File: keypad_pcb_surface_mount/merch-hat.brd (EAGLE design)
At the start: 65 x 56 mm, 29 parts, among them U2 ATMEGA328P_TQFP, Y2 16MHZ

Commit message: Fixes and updates
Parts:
- removed GPIO1: PIN20X2, FLYFISH:PIN_20X2
- removed PORT: Sensor Port, pinhead:1X03
- added C3: 0.1uF, merch-hardware:0603-CAP
- added PORT_OUT: Sensor Port, pinhead:1X03
- added R14: 1k, merch-hardware:0603-RES
- added R15, R16: 3.9k, merch-hardware:0603-RES
- added U1: CAT24C32, merch-hardware:SO08
- added WP: (no value), pinhead:1X02
- D2: value 74LS155D -> 74LS156D
- R1, R10, R11, R12, R13, R2, R3, R4, R5, R6, R7, R8, R9: device resistor:R0805 -> merch-hardware:0603-RES
- moved C1 20.5 mm to (29.7, 10.9), turned to 270 degrees
- moved R12 6.31 mm to (26.2, 42.3), turned to 90 degrees
- moved R13 5.99 mm to (28.8, 42.3), turned to 90 degrees
- moved LIMITSWITCH 5.99 mm to (26.2, 46.4), turned to 0 degrees
- moved R11 4.94 mm to (23.1, 34.8)
- moved C2 2.22 mm to (30.9, 14.9)
- moved R1 0.38 mm to (61.5, 13.2)
- moved R2 0.38 mm to (61.5, 15.7)
- moved R3 0.38 mm to (61.5, 18.3)
- moved R4 0.38 mm to (61.5, 20.8)
- moved R5 0.38 mm to (61.5, 23.4)
- moved R6 0.38 mm to (61.5, 25.9)
- moved R7 0.38 mm to (61.5, 31.0)
- moved R8 0.38 mm to (61.5, 33.5)
- moved R9 0.38 mm to (61.5, 36.1)
- renumbered COL_DEMUX to D2, ROW_MUX to D1, SELECT_BITS to D3
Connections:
- new net N$2: R14.1, U1.7, WP.1
- net +5V: no longer GPIO1.2, GPIO1.4
- net 3.3V: now also C3.2, R14.2, R15.2, R16.2, U1.8; no longer GPIO1.1, GPIO1.17
- net GND: now also C3.1, D2.14, PORT_OUT.3, U1.1, U1.2, U1.3, U1.4, WP.2; no longer GPIO1.14, GPIO1.20, GPIO1.25, GPIO1.30, GPIO1.34, GPIO1.39, GPIO1.6, GPIO1.9, PORT.3
- net GPIO10: no longer GPIO1.19
- net GPIO11: no longer GPIO1.23
- net GPIO12: no longer GPIO1.32
- net GPIO13: no longer GPIO1.33
- net GPIO16: now also D3.11; no longer GPIO1.36
- net GPIO19: no longer GPIO1.35
- net GPIO2: no longer GPIO1.3
- net GPIO20: now also PORT_OUT.1; no longer GPIO1.38, PORT.1
- net GPIO21: no longer GPIO1.40
- net GPIO23: now also LIMITSWITCH.1; no longer GPIO1.16, LIMITSWITCH.2
- net GPIO24: now also LIMITSWITCH.2; no longer GPIO1.18, LIMITSWITCH.1
- net GPIO25: no longer GPIO1.22
- net GPIO26: no longer GPIO1.37
- net GPIO3: no longer GPIO1.5
- net GPIO4: no longer GPIO1.7
- net GPIO5: now also D3.13; no longer GPIO1.29
- net GPIO6: no longer GPIO1.31
- net GPIO7: no longer GPIO1.26
- net GPIO8: no longer GPIO1.24
- net GPIO9: no longer GPIO1.21
- net ICSP_MISO: no longer GPIO1.13
- net ICSP_MOSI: no longer GPIO1.15
- net ICSP_RESET: no longer GPIO1.11
- net ICSP_SCK: no longer GPIO1.12
- net ID_SC: now also R15.1, U1.6; no longer GPIO1.28
- net ID_SD: now also R16.1, U1.5; no longer GPIO1.27
- net N$22: no longer D2.14
- net PI_RXD: no longer GPIO1.10
- net PI_TXD: no longer GPIO1.8
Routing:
- net +5V: track 202.0 -> 77.8 mm, vias 8 -> 7
- net GPIO16: track 6.43 -> 32.5 mm, vias 0 -> 2
- net ID_SC: track 6.43 -> 25.2 mm, vias 0 -> 1
- net GPIO5: track 6.43 -> 24.1 mm
- net 3.3V: track 12.9 -> 29.1 mm, vias 0 -> 1
- net ID_SD: track 6.43 -> 17.5 mm
- net N$2: track 0.00 -> 8.83 mm
- net GPIO20: track 17.1 -> 8.95 mm
- net GPIO23: track 19.3 -> 11.6 mm
- net GPIO24: track 18.8 -> 11.7 mm
- net GPIO12: track 6.43 -> 0.00 mm
- net GPIO25: track 6.43 -> 0.00 mm
- net GPIO11: track 6.43 -> 0.00 mm
- net GPIO9: track 6.43 -> 0.00 mm
- net GPIO8: track 6.43 -> 0.00 mm
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- added copper zone on layer 16, net +5V
- removed copper zone on layer 16, net GND
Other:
- board text added: "OUT"

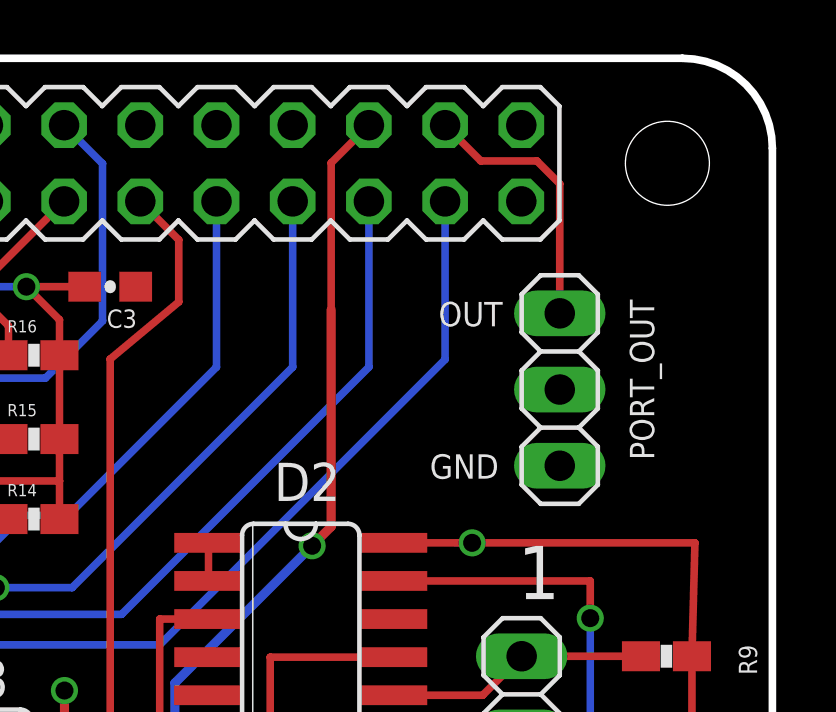
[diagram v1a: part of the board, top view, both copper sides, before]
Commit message: Change label, make vias circles
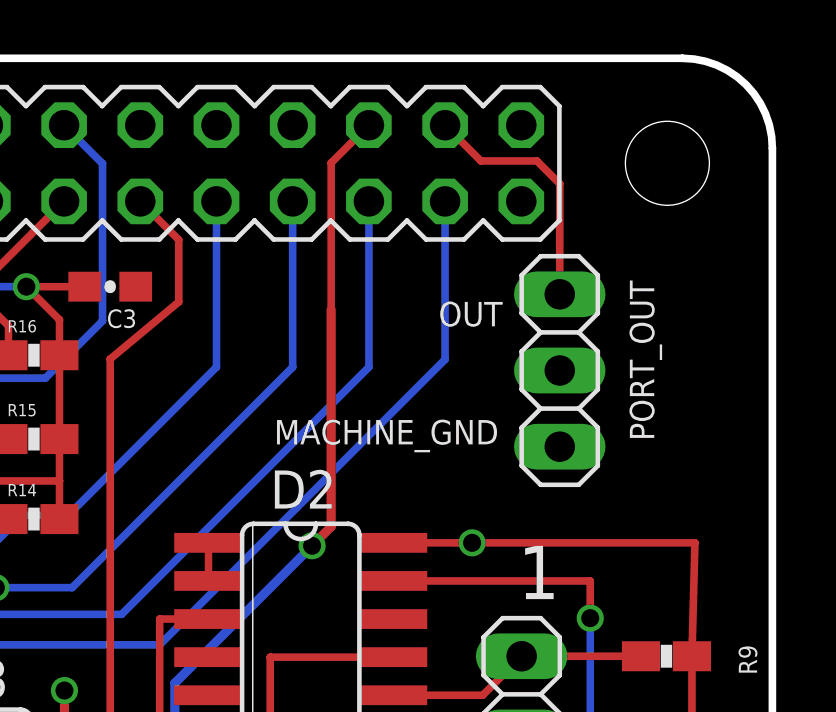
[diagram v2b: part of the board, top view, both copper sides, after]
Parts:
- moved PORT_OUT 0.64 mm to (57.9, 45.6)
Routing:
- net GPIO20: track 8.95 -> 8.31 mm
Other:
- board text added: "MACHINE_GND"
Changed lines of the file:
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@@
 <text x="11.811" y="28.067" size="1.27" layer="21">XSHD</text>
 <text x="46.863" y="6.35" size="1.778" layer="21">Merch v0.2</text>
-<text x="55.88" y="42.799" size="0.8128" layer="21" rot="R180">GND</text>
+<text x="55.88" y="43.942" size="0.8128" layer="21" rot="R180">MACHINE_GND</text>
 <text x="56.007" y="47.879" size="0.8128" layer="21" rot="R180">OUT</text>
 </plain>
@@
 </element>
 <element name="D2" library="74xx-us" package="SO16" value="74LS156D" x="49.278" y="35.403" smashed="yes" rot="R270">
-<attribute name="NAME" x="48.389" y="41.245" size="1.27" layer="25" ratio="10"/>
+<attribute name="NAME" x="48.262" y="40.991" size="1.27" layer="25" ratio="10"/>
 <attribute name="VALUE" x="48.643" y="39.467" size="1.27" layer="27" ratio="10" rot="R270"/>
 </element>
@@
 <attribute name="VALUE" x="6.477" y="42.545" size="1.27" layer="27" rot="R270"/>
 </element>
-<element name="PORT_OUT" library="pinhead" package="1X03" value="Sensor Port" x="57.912" y="44.958" smashed="yes" rot="R270">
-<attribute name="NAME" x="60.2488" y="47.9552" size="0.8128" layer="25" ratio="10" rot="R270"/>
-<attribute name="VALUE" x="54.737" y="48.768" size="1.27" layer="27" rot="R270"/>
+<element name="PORT_OUT" library="pinhead" package="1X03" value="Sensor Port" x="57.912" y="45.593" smashed="yes" rot="R270">
+<attribute name="NAME" x="60.2488" y="48.5902" size="0.8128" layer="25" ratio="10" rot="R270"/>
+<attribute name="VALUE" x="54.737" y="49.403" size="1.27" layer="27" rot="R270"/>
 </element>
 <element name="R10" library="merch-hardware" package="0603-RES" value="3.3k" x="41.402" y="20.701" smashed="yes" rot="R90">
@@
 <wire x1="27.559" y1="41.441" x2="28.829" y2="41.441" width="0.254" layer="1"/>
 <wire x1="54.453" y1="39.848" x2="54.991" y2="39.848" width="0.254" layer="16"/>
-<via x="54.991" y="39.848" extent="1-16" drill="0.6" shape="square"/>
+<via x="54.991" y="39.848" extent="1-16" drill="0.6"/>
 <polygon width="0.254" layer="16">
 <vertex x="0" y="3" curve="90"/>
@@
 </polygon>
 <wire x1="35.2806" y1="33.655" x2="32.893" y2="33.655" width="0.254" layer="1"/>
-<via x="32.893" y="33.655" extent="1-16" drill="0.6" shape="square"/>
+<via x="32.893" y="33.655" extent="1-16" drill="0.6"/>
 <wire x1="23.964" y1="34.798" x2="23.964" y2="33.401" width="0.254" layer="1"/>
 <wire x1="23.964" y1="33.401" x2="24.003" y2="33.401" width="0.254" layer="1"/>
-<via x="24.003" y="33.401" extent="1-16" drill="0.6" shape="square"/>
-<via x="27.559" y="40.132" extent="1-16" drill="0.6" shape="square"/>
+<via x="24.003" y="33.401" extent="1-16" drill="0.6"/>
+<via x="27.559" y="40.132" extent="1-16" drill="0.6"/>
 <wire x1="27.559" y1="40.132" x2="27.559" y2="41.441" width="0.254" layer="1"/>
 <wire x1="25.654" y1="15.907" x2="27.7876" y2="15.907" width="0.6096" layer="1"/>
-<via x="21.463" y="17.653" extent="1-16" drill="0.6" shape="square"/>
+<via x="21.463" y="17.653" extent="1-16" drill="0.6"/>
 <wire x1="21.463" y1="16.707" x2="19.2024" y2="16.707" width="0.6096" layer="1"/>
 <wire x1="21.463" y1="16.707" x2="25.654" y2="16.707" width="0.6096" layer="1"/>
@@
 <wire x1="40.005" y1="40.767" x2="41.529" y2="40.767" width="0.254" layer="16"/>
 <wire x1="41.529" y1="40.767" x2="46.47" y2="45.708" width="0.254" layer="16"/>
-<via x="34.036" y="34.798" extent="1-16" drill="0.6" shape="square"/>
+<via x="34.036" y="34.798" extent="1-16" drill="0.6"/>
 <wire x1="31.242" y1="31.115" x2="31.242" y2="26.416" width="0.254" layer="1"/>
 <wire x1="31.242" y1="26.416" x2="34.417" y2="23.241" width="0.254" layer="1"/>
@@
 <wire x1="54.09" y1="53.77" x2="55.282" y2="52.578" width="0.254" layer="1"/>
 <wire x1="57.15" y1="52.578" x2="57.912" y2="51.816" width="0.254" layer="1"/>
-<wire x1="57.912" y1="51.816" x2="57.912" y2="47.498" width="0.254" layer="1"/>
+<wire x1="57.912" y1="51.816" x2="57.912" y2="48.133" width="0.254" layer="1"/>
 <wire x1="55.282" y1="52.578" x2="57.15" y2="52.578" width="0.254" layer="1"/>
 </signal>
@@
 <wire x1="41.4274" y1="27.305" x2="43.18" y2="27.305" width="0.254" layer="1"/>
 <wire x1="43.18" y1="27.305" x2="43.434" y2="27.051" width="0.254" layer="1"/>
-<via x="43.434" y="27.051" extent="1-16" drill="0.6" shape="square"/>
+<via x="43.434" y="27.051" extent="1-16" drill="0.6"/>
 <wire x1="43.434" y1="27.051" x2="43.942" y2="27.051" width="0.254" layer="16"/>
 <wire x1="43.942" y1="27.051" x2="45.085" y2="28.194" width="0.254" layer="16"/>
